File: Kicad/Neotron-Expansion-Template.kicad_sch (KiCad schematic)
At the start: 26 parts, among them U1 MCP23S17

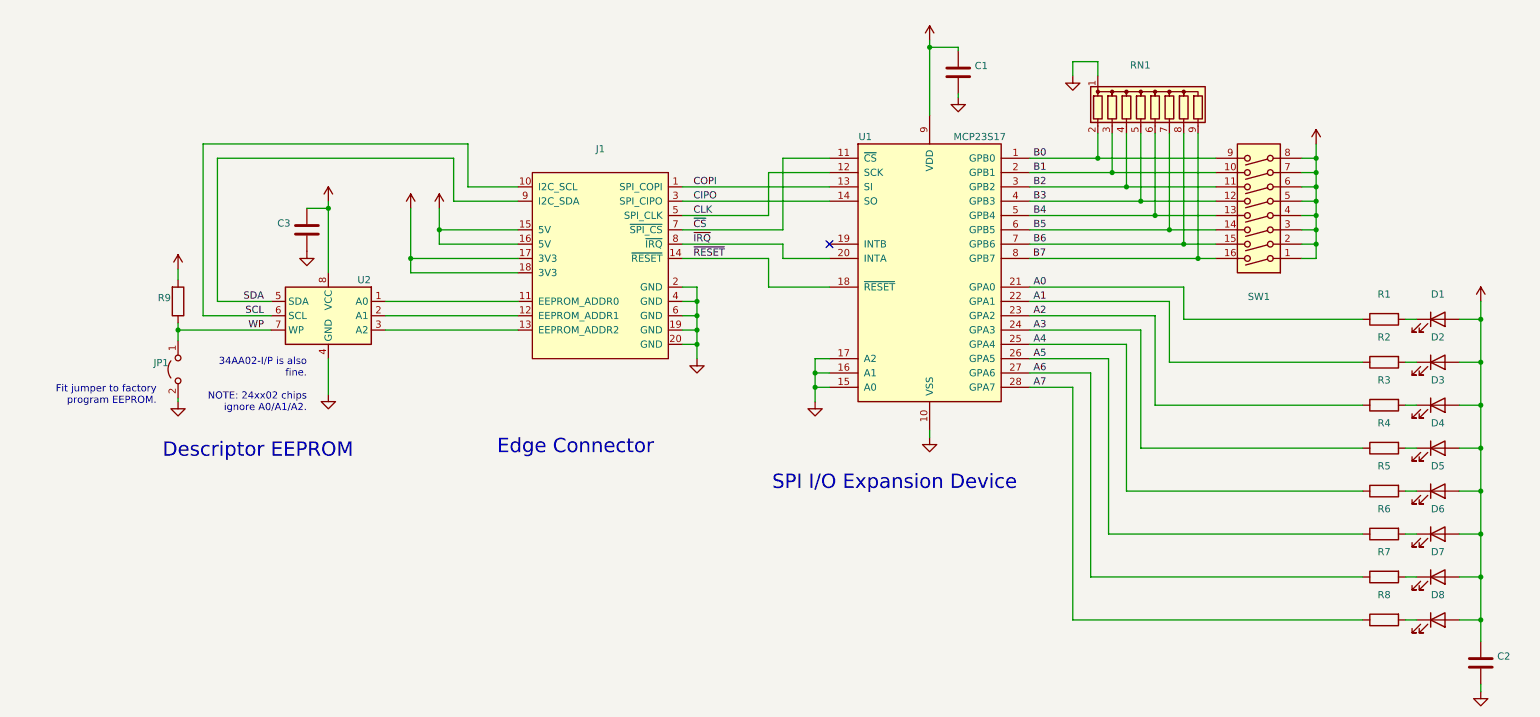
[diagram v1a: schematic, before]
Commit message: Adjusted board size to suit Neotron Pico 1.0.0.
Has holes for a random backplate I found.
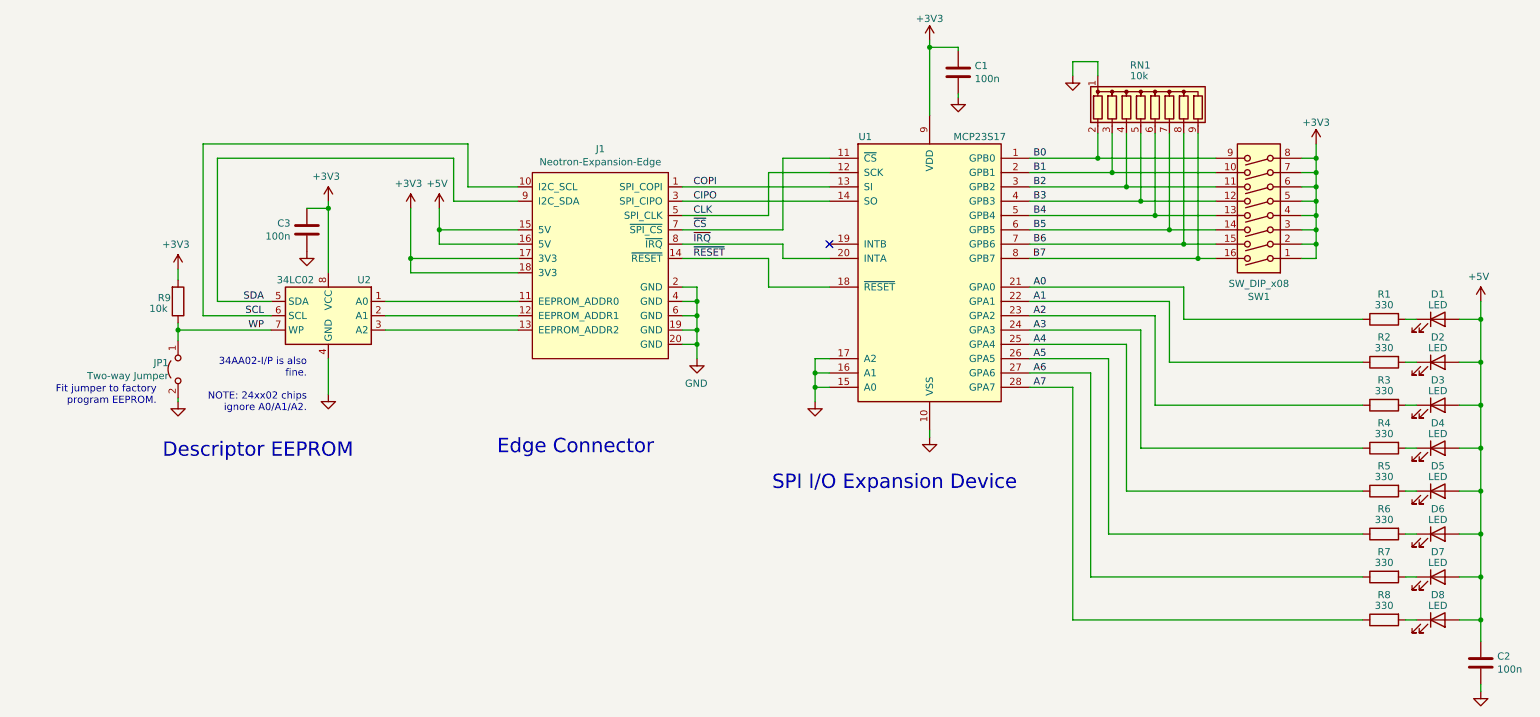
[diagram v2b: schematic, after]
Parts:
- C1, C2, C3: value (none) -> 100n; footprint (none) -> Capacitor_THT:C_Disc_D7.0mm_W2.5mm_P5.00mm
- D1, D2, D3, D4, D5, D6, D7, D8: value (none) -> LED; footprint (none) -> LED_THT:LED_D3.0mm
- J1: value (none) -> Neotron-Expansion-Edge; footprint (none) -> Neotron-Common-Hardware:Neotron-Expansion-Edge
- JP1: value (none) -> Two-way Jumper; footprint (none) -> Connector_PinHeader_2.54mm:PinHeader_1x02_P2.54mm_Vertical
- R1, R2, R3, R4, R5, R6, R7, R8: value (none) -> 330; footprint (none) -> Resistor_THT:R_Axial_DIN0207_L6.3mm_D2.5mm_P10.16mm_Horizontal
- R9: value (none) -> 10k; footprint (none) -> Resistor_THT:R_Axial_DIN0207_L6.3mm_D2.5mm_P10.16mm_Horizontal
- RN1: value (none) -> 10k; footprint (none) -> Resistor_THT:R_Array_SIP9
- SW1: value (none) -> SW_DIP_x08; footprint (none) -> Package_DIP:DIP-16_W7.62mm_LongPads
- U2: value (none) -> 34LC02; footprint (none) -> Package_DIP:DIP-8_W7.62mm

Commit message: Fix DRC issues.
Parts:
- added H1, H2: MountingHole_Pad, MountingHole:MountingHole_2.7mm_M2.5_Pad, symbol Mechanical:MountingHole_Pad
- renumbered C3 to C2, C2 to C3, R9 to R1, R1 to R2, R2 to R3, R3 to R4, R4 to R5, R5 to R6, R6 to R7, R7 to R8, R8 to R9
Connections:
- net GND: now also H1.1, H2.1
